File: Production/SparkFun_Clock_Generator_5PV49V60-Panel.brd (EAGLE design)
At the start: 133.3 x 200.9 mm, 2162 parts, among them J1 QWIIC_RIGHT_ANGLE, J100 QWIIC_RIGHT_ANGLE, J106 QWIIC_RIGHT_ANGLE, J107 QWIIC_RIGHT_ANGLE, J113 QWIIC_RIGHT_ANGLE, J114 QWIIC_RIGHT_ANGLE, J120 QWIIC_RIGHT_ANGLE, J121 QWIIC_RIGHT_ANGLE, J127 QWIIC_RIGHT_ANGLE, J128 QWIIC_RIGHT_ANGLE, J134 QWIIC_RIGHT_ANGLE, J135 QWIIC_RIGHT_ANGLE, J141 QWIIC_RIGHT_ANGLE, J142 QWIIC_RIGHT_ANGLE, J148 QWIIC_RIGHT_ANGLE, J149 QWIIC_RIGHT_ANGLE, J15 QWIIC_RIGHT_ANGLE, J155 QWIIC_RIGHT_ANGLE, J156 QWIIC_RIGHT_ANGLE, J16 QWIIC_RIGHT_ANGLE, J162 QWIIC_RIGHT_ANGLE, J163 QWIIC_RIGHT_ANGLE, J169 QWIIC_RIGHT_ANGLE, J170 QWIIC_RIGHT_ANGLE, J176 QWIIC_RIGHT_ANGLE, J177 QWIIC_RIGHT_ANGLE, J183 QWIIC_RIGHT_ANGLE, J184 QWIIC_RIGHT_ANGLE, J190 QWIIC_RIGHT_ANGLE, J191 QWIIC_RIGHT_ANGLE, J2 QWIIC_RIGHT_ANGLE, J22 QWIIC_RIGHT_ANGLE, J23 QWIIC_RIGHT_ANGLE, J29 QWIIC_RIGHT_ANGLE, J30 QWIIC_RIGHT_ANGLE, J36 QWIIC_RIGHT_ANGLE, J37 QWIIC_RIGHT_ANGLE, J43 QWIIC_RIGHT_ANGLE, J44 QWIIC_RIGHT_ANGLE, J50 QWIIC_RIGHT_ANGLE, J51 QWIIC_RIGHT_ANGLE, J57 QWIIC_RIGHT_ANGLE, J58 QWIIC_RIGHT_ANGLE, J6 QWIIC_RIGHT_ANGLE, J64 QWIIC_RIGHT_ANGLE, J65 QWIIC_RIGHT_ANGLE, J71 QWIIC_RIGHT_ANGLE, J72 QWIIC_RIGHT_ANGLE, J78 QWIIC_RIGHT_ANGLE, J79 QWIIC_RIGHT_ANGLE, J85 QWIIC_RIGHT_ANGLE, J86 QWIIC_RIGHT_ANGLE, J9 QWIIC_RIGHT_ANGLE, J92 QWIIC_RIGHT_ANGLE, J93 QWIIC_RIGHT_ANGLE, J99 QWIIC_RIGHT_ANGLE, U1 IDT_5P49V60_CLOCK_GENERATOR, U10 IDT_5P49V60_CLOCK_GENERATOR, U11 IDT_5P49V60_CLOCK_GENERATOR, U12 IDT_5P49V60_CLOCK_GENERATOR, U13 IDT_5P49V60_CLOCK_GENERATOR, U14 IDT_5P49V60_CLOCK_GENERATOR, U15 IDT_5P49V60_CLOCK_GENERATOR, U16 IDT_5P49V60_CLOCK_GENERATOR, U17 IDT_5P49V60_CLOCK_GENERATOR, U18 IDT_5P49V60_CLOCK_GENERATOR, U19 IDT_5P49V60_CLOCK_GENERATOR, U2 IDT_5P49V60_CLOCK_GENERATOR, U20 IDT_5P49V60_CLOCK_GENERATOR, U21 IDT_5P49V60_CLOCK_GENERATOR, U22 IDT_5P49V60_CLOCK_GENERATOR, U23 IDT_5P49V60_CLOCK_GENERATOR, U24 IDT_5P49V60_CLOCK_GENERATOR, U25 IDT_5P49V60_CLOCK_GENERATOR, U26 IDT_5P49V60_CLOCK_GENERATOR, U27 IDT_5P49V60_CLOCK_GENERATOR, U28 IDT_5P49V60_CLOCK_GENERATOR, U3 IDT_5P49V60_CLOCK_GENERATOR, U4 IDT_5P49V60_CLOCK_GENERATOR, U5 IDT_5P49V60_CLOCK_GENERATOR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

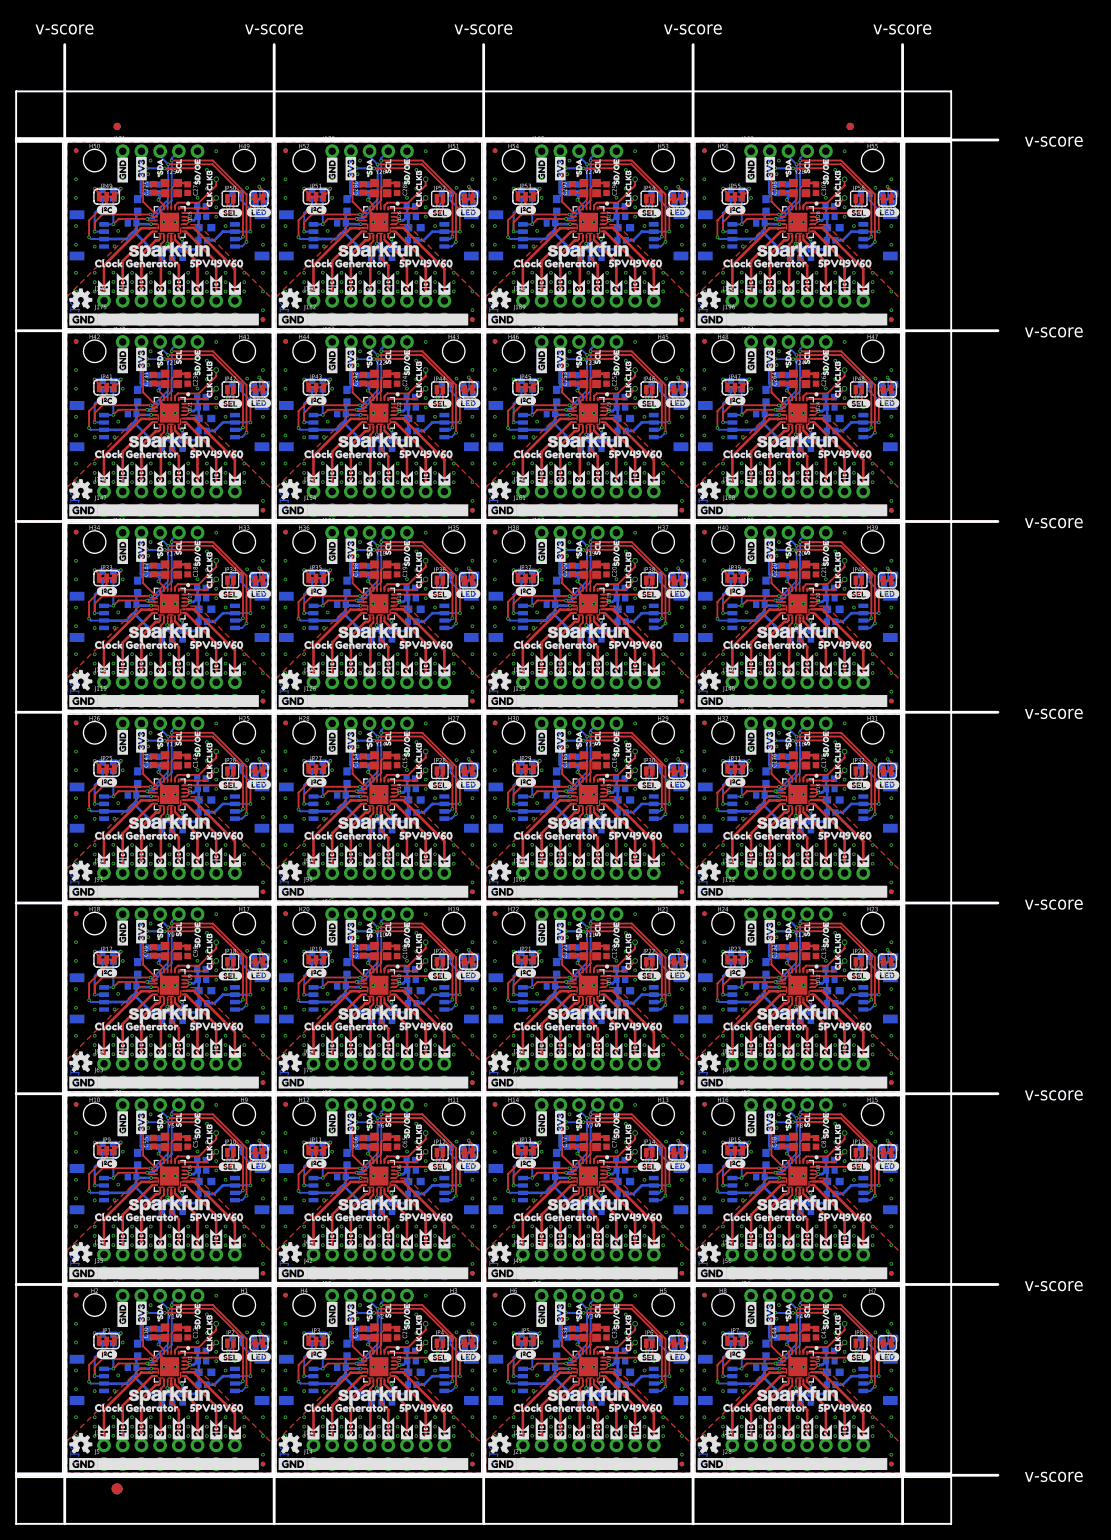
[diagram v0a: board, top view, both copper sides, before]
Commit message: Replaces previous panel due to the Panelizer changing the DRC
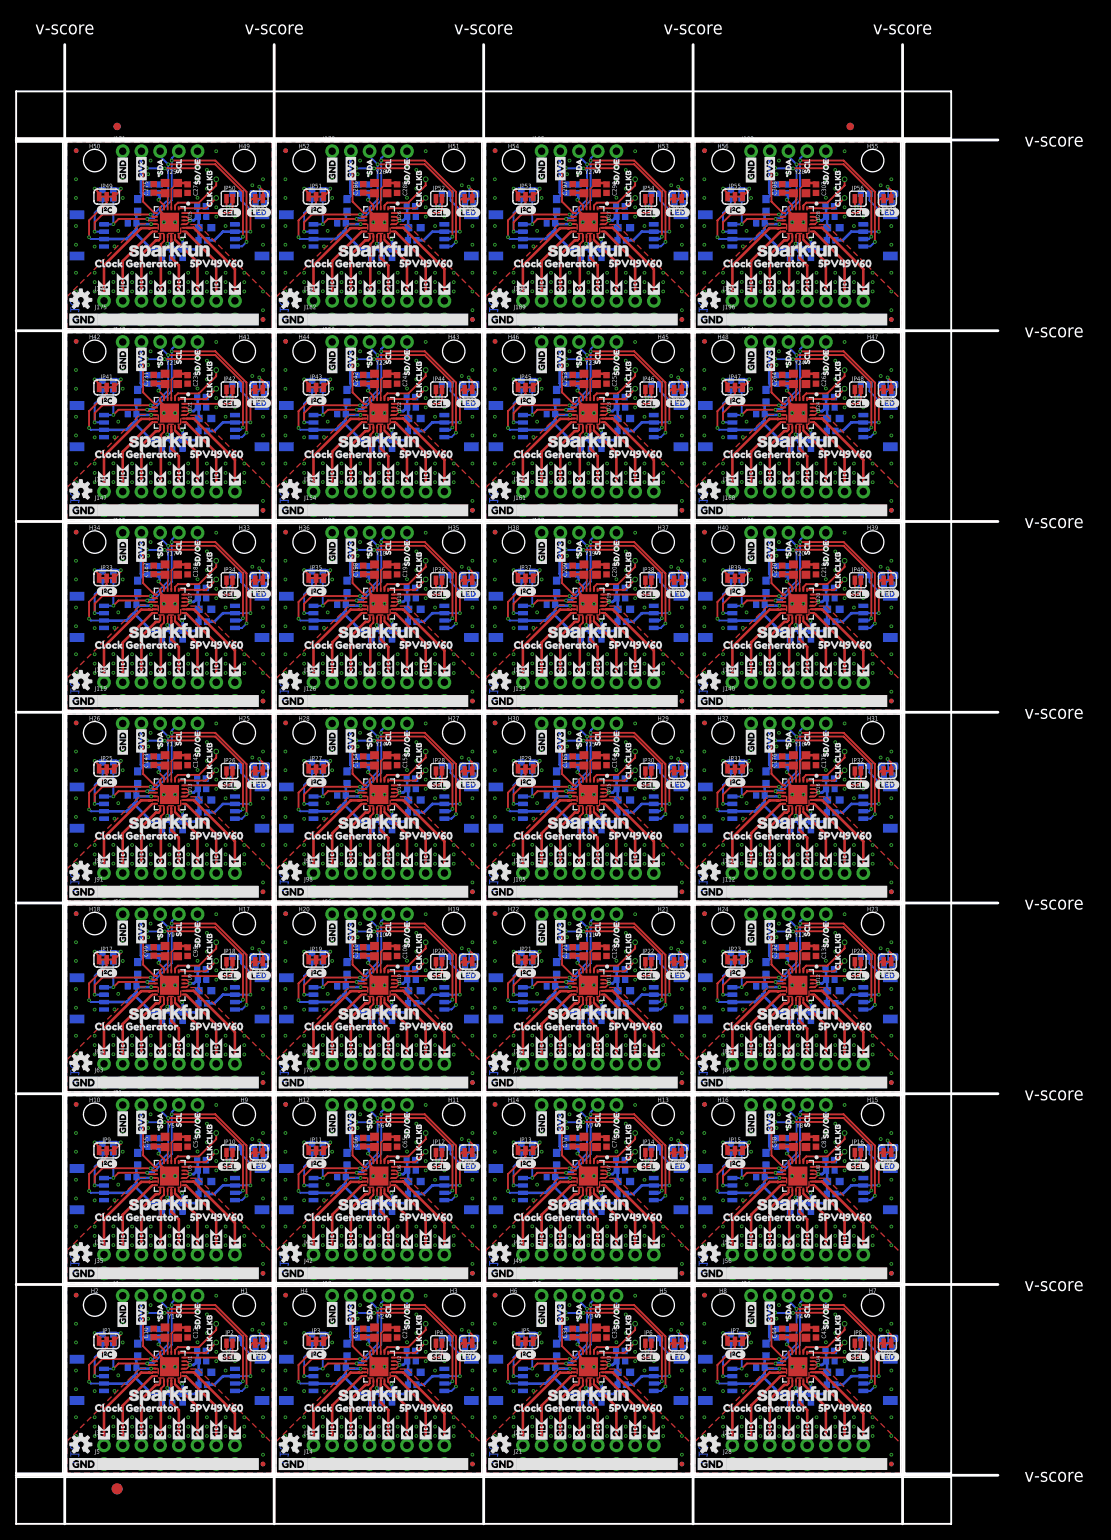
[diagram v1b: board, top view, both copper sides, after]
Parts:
- moved LOGO66 0.22 mm to (54.0, 137.8)
- moved LOGO69 0.22 mm to (82.5, 137.8)
- moved LOGO78 0.22 mm to (54.0, 163.7)
- moved LOGO81 0.22 mm to (82.5, 163.7)
- moved LOGO63 0.22 mm to (25.6, 137.8)
- moved LOGO75 0.22 mm to (25.6, 163.7)
- moved LOGO18 0.22 mm to (54.0, 34.2)
- moved LOGO21 0.22 mm to (82.5, 34.2)
- moved LOGO30 0.22 mm to (54.0, 60.1)
- moved LOGO33 0.22 mm to (82.5, 60.1)
- moved LOGO6 0.22 mm to (54.0, 8.26)
- moved LOGO9 0.22 mm to (82.5, 8.26)
- moved LOGO15 0.22 mm to (25.6, 34.2)
- moved LOGO27 0.22 mm to (25.6, 60.1)
- moved LOGO42 0.22 mm to (54.0, 86.0)
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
